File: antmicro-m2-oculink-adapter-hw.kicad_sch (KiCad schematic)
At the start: 21 parts, among them J1 PCB-Edge_M.2_Key-M, J2 OCuLink_x4_Amphenol_G14A42121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

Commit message: [#81131] Clean drc
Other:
- moved on the sheet: C1, C2, C3, C4, J1, J2, R1, R10, R11, R2, R3, R4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

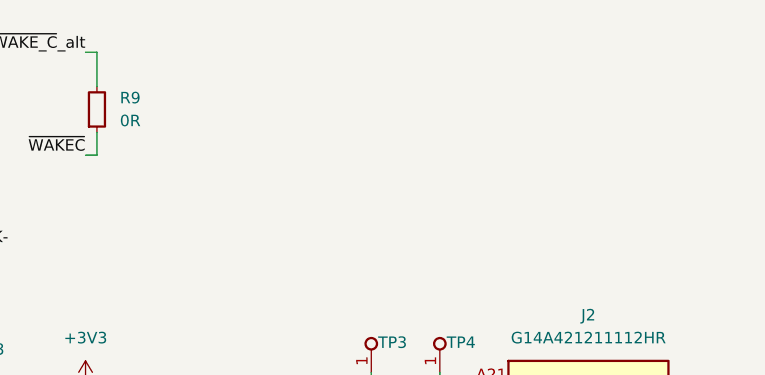
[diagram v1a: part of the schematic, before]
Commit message: [#81131] Clean-up tracks, shorten stubs, relocate R1, align silkscreen
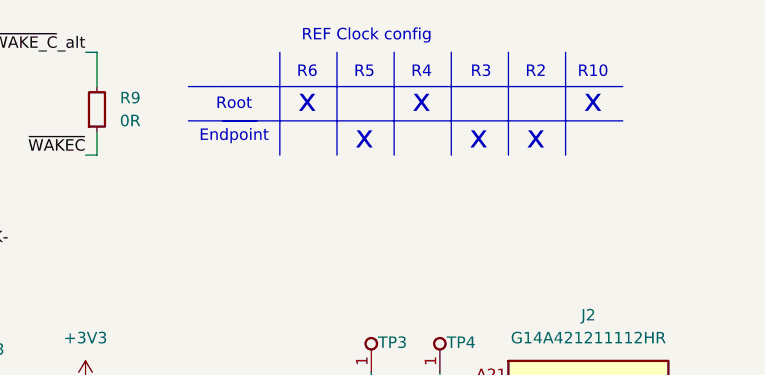
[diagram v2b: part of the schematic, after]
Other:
- note added: "Endpoint"
- note added: "R10"
- note added: "R2"
- note added: "R3"
- note added: "R4"
- note added: "R5"
- note added: "R6"
- note added: "REF Clock config"
- note added: "Root"
- note added: "x"
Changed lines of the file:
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@@
 		(comment 1 "www.antmicro.com")
+	)
+	(text "REF Clock config"
+		(exclude_from_sim no)
+		(at 234.442 21.082 0)
+		(effects
+			(font
+				(size 1.27 1.27)
+			)
+		)
+	)
+	(text "Endpoint\n"
+		(exclude_from_sim no)
+		(at 219.71 32.258 0)
+		(effects
+			(font
+				(size 1.27 1.27)
+			)
+		)
+	)
+	(text "x"
+		(exclude_from_sim no)
+		(at 246.888 32.512 0)
+		(effects
+			(font
+				(size 2.54 2.54)
+			)
+		)
+	)
+	(text "R6\n"
+		(exclude_from_sim no)
+		(at 227.838 25.146 0)
+		(effects
+			(font
+				(size 1.27 1.27)
+			)
+		)
+	)
+	(text "Root"
+		(exclude_from_sim no)
+		(at 219.71 28.702 0)
+		(effects
+			(font
+				(size 1.27 1.27)
+			)
+		)
+	)
+	(text "x"
+		(exclude_from_sim no)
+		(at 240.538 28.448 0)
+		(effects
+			(font
+				(size 2.54 2.54)
+			)
+		)
+	)
+	(text "x"
+		(exclude_from_sim no)
+		(at 259.588 28.448 0)
+		(effects
+			(font
+				(size 2.54 2.54)
+			)
+		)
+	)
+	(text "x"
+		(exclude_from_sim no)
+		(at 234.188 32.512 0)
+		(effects
+			(font
+				(size 2.54 2.54)
+			)
+		)
+	)
+	(text "x"
+		(exclude_from_sim no)
+		(at 227.838 28.448 0)
+		(effects
+			(font
+				(size 2.54 2.54)
+			)
+		)
+	)
+	(text "R3"
+		(exclude_from_sim no)
+		(at 247.142 25.146 0)
+		(effects
+			(font
+				(size 1.27 1.27)
+			)
+		)
+	)
+	(text "R4"
+		(exclude_from_sim no)
+		(at 240.538 25.146 0)
+		(effects
+			(font
+				(size 1.27 1.27)
+			)
+		)
+	)
+	(text "x"
+		(exclude_from_sim no)
+		(at 253.238 32.512 0)
+		(effects
+			(font
+				(size 2.54 2.54)
+			)
+		)
+	)
+	(text "R5"
+		(exclude_from_sim no)
+		(at 234.188 25.146 0)
+		(effects
+			(font
+				(size 1.27 1.27)
+			)
+		)
+	)
+	(text "R2"
+		(exclude_from_sim no)
+		(at 253.238 25.146 0)
+		(effects
+			(font
+				(size 1.27 1.27)
+			)
+		)
+	)
+	(text "R10\n"
+		(exclude_from_sim no)
+		(at 259.588 25.146 0)
+		(effects
+			(font
+				(size 1.27 1.27)
+			)
+		)
 	)
 	(junction
@@
 		)
 	)
+	(polyline
+		(pts
+			(xy 214.63 30.48) (xy 222.25 30.48)
+		)
+		(stroke
+			(width 0)
+			(type default)
+		)
+	)
 	(bus
 		(pts
@@
 		)
 	)
+	(polyline
+		(pts
+			(xy 231.14 22.86) (xy 231.14 34.29)
+		)
+		(stroke
+			(width 0)
+			(type default)
+		)
+	)
 	(wire
 		(pts
@@
 		)
 	)
+	(polyline
+		(pts
+			(xy 218.44 26.67) (xy 262.89 26.67)
+		)
+		(stroke
+			(width 0)
+			(type default)
+		)
+	)
 	(wire
 		(pts
@@
 		)
 	)
+	(polyline
+		(pts
+			(xy 250.19 22.86) (xy 250.19 34.29)
+		)
+		(stroke
+			(width 0)
+			(type default)
+		)
+	)
 	(wire
 		(pts
@@
 		)
 	)
+	(polyline
+		(pts
+			(xy 243.84 22.86) (xy 243.84 34.29)
+		)
+		(stroke
+			(width 0)
+			(type default)
+		)
+	)
 	(bus
 		(pts
@@
 		)
 	)
+	(polyline
+		(pts
+			(xy 256.54 22.86) (xy 256.54 34.29)
+		)
+		(stroke
+			(width 0)
+			(type default)
+		)
+	)
 	(wire
 		(pts
@@
 		)
 	)
+	(polyline
+		(pts
+			(xy 218.44 30.48) (xy 262.89 30.48)
+		)
+		(stroke
+			(width 0)
+			(type default)
+		)
+	)
 	(wire
 		(pts
@@
 		)
 	)
+	(polyline
+		(pts
+			(xy 218.44 26.67) (xy 214.63 26.67)
+		)
+		(stroke
+			(width 0)
+			(type default)
+		)
+	)
 	(bus
 		(pts
@@
 		)
 	)
+	(polyline
+		(pts
+			(xy 224.79 22.86) (xy 224.79 34.29)
+		)
+		(stroke
+			(width 0)
+			(type default)
+		)
+	)
 	(wire
 		(pts
@@
 		)
 		(stroke
+			(width 0)
+			(type default)
+		)
+	)
+	(polyline
+		(pts
+			(xy 237.49 22.86) (xy 237.49 34.29)
+		)
+		(stroke

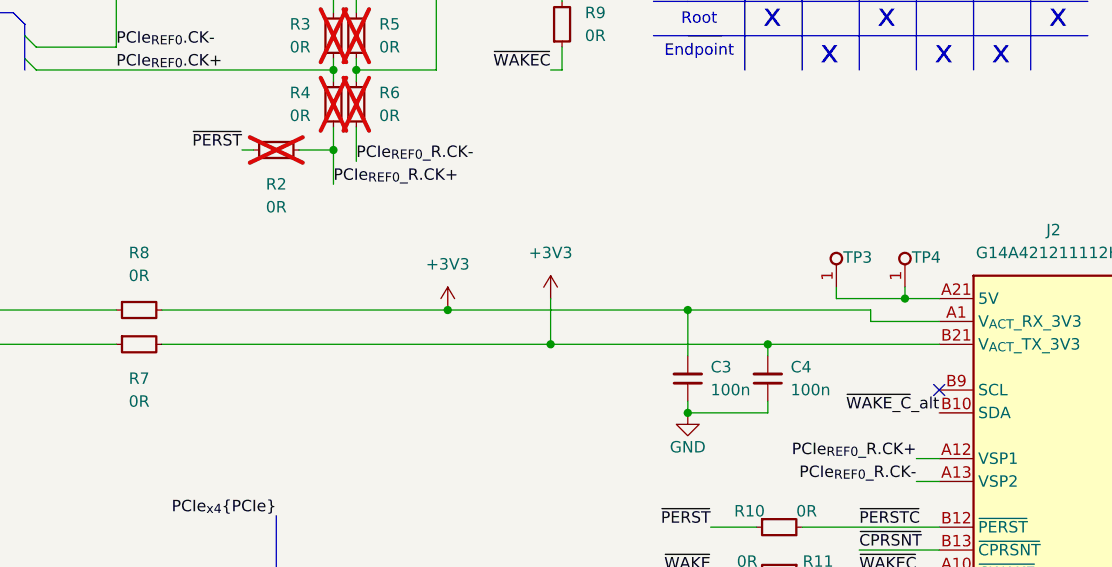
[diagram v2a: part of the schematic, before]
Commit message: [#81131] Add 0R on 5V, Clean drc
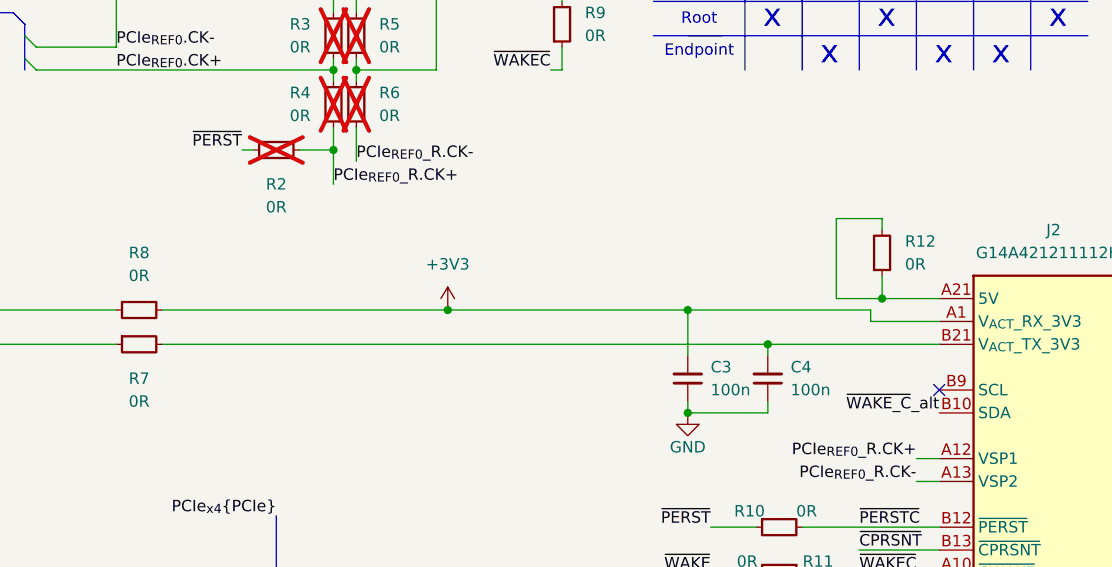
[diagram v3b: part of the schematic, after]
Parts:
- removed TP3, TP4: TP_1.5mm_SMD, antmicro-footprints:TP_SMD_1.5mm, symbol TestPoints:TP_1.5mm_SMD
- added R12: R_0R_0201, antmicro-footprints:R_0201, symbol antmicroResistorsmisc:R_0R_0201
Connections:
- net +3V3: no longer C4.2, J2.B21 (V_{ACT}_TX_3V3), R7.2
- net at J2.A21 (5V), J2.B1 (5V): now also R12.1, R12.2
- new net: C4.2, J2.B21 (V_{ACT}_TX_3V3), R7.2

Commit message: [#81131] Increase silkscreen spacing, add gnd cutouts to vias, increase distance drill to traces, remove solder mask from m.2 connector
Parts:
- removed R12: R_0R_0201, antmicro-footprints:R_0201, symbol antmicroResistorsmisc:R_0R_0201
- added R12: R_0R_0402, antmicro-footprints:R_0402_1005Metric, symbol Resistors0402:R_0R_0402
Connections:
- net at J2.A21 (5V), J2.B1 (5V): now also R12.1, R12.2
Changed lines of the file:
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@@
 		(title " M.2 to OCuLink adapter")
 		(date "2025-07-09")
-		(rev "1.0.0")
+		(rev "1.0.1")
 		(company "Antmicro Ltd")
 		(comment 1 "www.antmicro.com")
@@
 	)
 	(symbol
-		(lib_id "antmicroResistorsmisc:R_0R_0201")
-		(at 240.03 57.15 90)
-		(unit 1)
-		(exclude_from_sim no)
-		(in_bom yes)
-		(on_board yes)
-		(dnp no)
-		(fields_autoplaced yes)
-		(property "Reference" "R12"
-			(at 242.57 53.34 90)
-			(effects
-				(font
-					(size 1.27 1.27)
-					(thickness 0.15)
-				)
-				(justify right)
-			)
-		)
-		(property "Value" "R_0R_0201"
-			(at 252.73 36.83 0)
-			(effects
-				(font
-					(size 1.27 1.27)
-					(thickness 0.15)
-				)
-				(justify left bottom)
-				(hide yes)
-			)
-		)
-		(property "Footprint" "antmicro-footprints:R_0201"
-			(at 255.27 36.83 0)
-			(effects
-				(font
-					(size 1.27 1.27)
-					(thickness 0.15)
-				)
-				(justify left bottom)
-				(hide yes)
-			)
-		)
-		(property "Datasheet" "https://www.bourns.com/docs/product-datasheets/cr.pdf"
-			(at 257.81 36.83 0)
-			(effects
-				(font
-					(size 1.27 1.27)
-					(thickness 0.15)
-				)
-				(justify left bottom)
-				(hide yes)
-			)
-		)
-		(property "Description" "SMD Chip Resistor"
-			(at 240.03 57.15 0)
-			(effects
-				(font
-					(size 1.27 1.27)
-				)
-				(hide yes)
-			)
-		)
-		(property "MPN" "CR0201-FX-0R00GLF"
-			(at 260.35 36.83 0)
-			(effects
-				(font
-					(size 1.27 1.27)
-					(thickness 0.15)
-				)
-				(justify left bottom)
-				(hide yes)
-			)
-		)
-		(property "Manufacturer" "Bourns"
-			(at 262.89 36.83 0)
-			(effects
-				(font
-					(size 1.27 1.27)
-					(thickness 0.15)
-				)
-				(justify left bottom)
-				(hide yes)
-			)
-		)
-		(property "License" "Apache-2.0"
-			(at 265.43 36.83 0)
-			(effects
-				(font
-					(size 1.27 1.27)
-					(thickness 0.15)
-				)
-				(justify left bottom)
-				(hide yes)
-			)
-		)
-		(property "Author" "Antmicro"
-			(at 267.97 36.83 0)
-			(effects
-				(font
-					(size 1.27 1.27)
-					(thickness 0.15)
-				)
-				(justify left bottom)
-				(hide yes)
-			)
-		)
-		(property "Val" "0R"
-			(at 242.57 55.88 90)
-			(effects
-				(font
-					(size 1.27 1.27)
-					(thickness 0.15)
-				)
-				(justify right)
-			)
-		)
-		(property "Tolerance" "1%"
-			(at 250.19 36.83 0)
-			(effects
-				(font
-					(size 1.27 1.27)
-				)
-				(justify left bottom)
-				(hide yes)
-			)
-		)
-		(pin "2"
-		)
-		(pin "1"
-		)
-		(instances
-			(project "antmicro-m2-oculink-adapter-hw"
-				(path "/b9cca87b-aef2-493b-be4f-d9e02584eafa"
-					(reference "R12")
-					(unit 1)
-				)
-			)
-		)
-	)
-	(symbol
 		(lib_id "power:+3V3")
 		(at 191.77 60.96 0)
@@
 					(unit 1)
 				)
+			)
+		)
+	)
+	(symbol
+		(lib_id "Resistors0402:R_0R_0402")
+		(at 240.03 57.15 90)
+		(unit 1)
+		(exclude_from_sim no)
+		(in_bom yes)
+		(on_board yes)
+		(dnp no)
+		(fields_autoplaced yes)
+		(property "Reference" "R12"
+			(at 242.57 53.34 90)
+			(effects
+				(font
+					(size 1.27 1.27)
+					(thickness 0.15)
+				)
+				(justify right)
+			)
+		)
+		(property "Value" "R_0R_0402"
+			(at 252.73 36.83 0)
+			(effects
+				(font
+					(size 1.27 1.27)
+					(thickness 0.15)
+				)
+				(justify left bottom)
+				(hide yes)
+			)
+		)
+		(property "Footprint" "antmicro-footprints:R_0402_1005Metric"
+			(at 255.27 36.83 0)
+			(effects
+				(font
+					(size 1.27 1.27)
+					(thickness 0.15)
+				)
+				(justify left bottom)
+				(hide yes)
+			)
+		)
+		(property "Datasheet" "https://industrial.panasonic.com/cdbs/www-data/pdf/RDA0000/AOA0000C301.pdf"
+			(at 257.81 36.83 0)
+			(effects
+				(font
+					(size 1.27 1.27)
+					(thickness 0.15)
+				)
+				(justify left bottom)
+				(hide yes)
+			)
+		)
+		(property "Description" "SMD Chip Resistor, Jumper, 0 ohm, 100 mW, 0402 [1005 Metric], Thick Film, General Purpose"
+			(at 240.03 57.15 0)
+			(effects
+				(font
+					(size 1.27 1.27)
+				)
+				(hide yes)
+			)
+		)
+		(property "MPN" "ERJ2GE0R00X"
+			(at 260.35 36.83 0)
+			(effects
+				(font
+					(size 1.27 1.27)
+					(thickness 0.15)
+				)
+				(justify left bottom)
+				(hide yes)
+			)
+		)
+		(property "Manufacturer" "Panasonic"
+			(at 262.89 36.83 0)
+			(effects
+				(font
+					(size 1.27 1.27)
+					(thickness 0.15)
+				)
+				(justify left bottom)
+				(hide yes)
+			)
+		)
+		(property "License" "Apache-2.0"
+			(at 265.43 36.83 0)
+			(effects
+				(font
+					(size 1.27 1.27)
+					(thickness 0.15)
+				)
+				(justify left bottom)
+				(hide yes)
+			)
+		)
+		(property "Author" "Antmicro"
+			(at 267.97 36.83 0)
+			(effects
+				(font
+					(size 1.27 1.27)
+					(thickness 0.15)
+				)
+				(justify left bottom)
+				(hide yes)
+			)
+		)
+		(property "Val" "0R"
+			(at 242.57 55.88 90)
+			(effects
+				(font
+					(size 1.27 1.27)
+					(thickness 0.15)
+				)
+				(justify right)
+			)
+		)
+		(property "Tolerance" "~"
+			(at 250.19 36.83 0)
+			(effects
+				(font
+					(size 1.27 1.27)
+				)
+				(justify left bottom)
+				(hide yes)
+			)
+		)
+		(property "Current" "1A"
+			(at 270.51 36.83 0)
+			(effects
+				(font
+					(size 1.27 1.27)
+					(thickness 0.15)
+				)
+				(justify left bottom)
+				(hide yes)
+			)
+		)
+		(pin "2"
+		)
+		(pin "1"
+		)
+		(instances
+			(project "antmicro-m2-oculink-adapter-hw"
+				(path "/b9cca87b-aef2-493b-be4f-d9e02584eafa"
+					(reference "R12")
+					(unit 1)
+				)

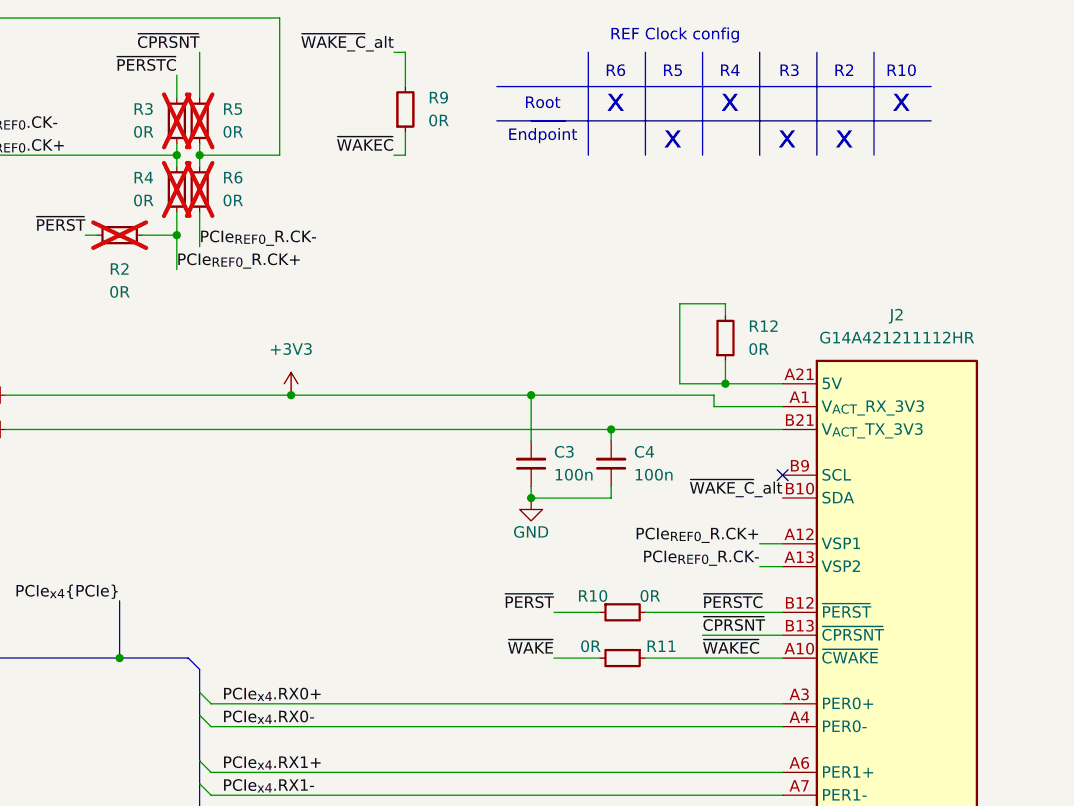
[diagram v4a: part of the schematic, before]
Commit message: [#81131] remove silkscreen from revision, add testpoint to CPRSNT
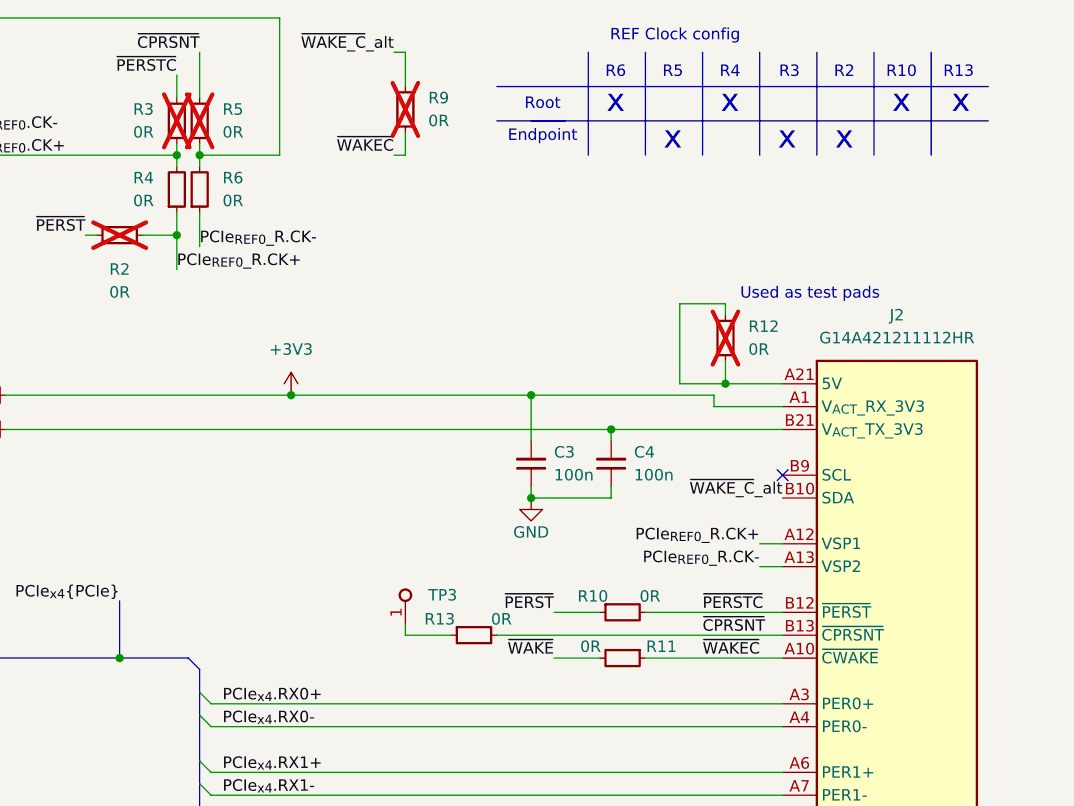
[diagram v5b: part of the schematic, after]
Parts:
- added R13: R_0R_0201, antmicro-footprints:R_0201, symbol antmicroResistorsmisc:R_0R_0201
- added TP3: TP_1mm_SMD, antmicro-footprints:TP_SMD_1mm, symbol antmicroTestPoints:TP_1mm_SMD
- R12, R9: now not fitted
- R4, R6: now fitted
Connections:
- net ~{CPRSNT}: now also R13.2
- new net: R13.1, TP3.1
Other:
- note added: "R13"
- note added: "Used as test pads"
